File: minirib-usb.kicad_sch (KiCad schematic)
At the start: 59 parts, among them J1 USB_B_Micro, J2 Mini-DIN-6-Shielded, J3 RS232, Q1 MMBT3906, Q2 MMBT3904, Q3 MMBT3904, Q4 MMBT3904, Q5 MMBT3906, Q6 MMBT3904, Q7 MMBT3904, Q8 BSS138W, U1 FT231XS, U2 TL071, U3 MAX232

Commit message: initial revision D updates
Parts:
- removed C2, C6, C7, C8, C9: 1uF, Capacitor_SMD:C_0805_2012Metric_Pad1.18x1.45mm_HandSolder, symbol Device:C_Small
- removed C5: 0.1uF, Capacitor_SMD:C_0805_2012Metric_Pad1.18x1.45mm_HandSolder, symbol Device:C_Small
- removed D5, D6, D7: 1N4148, Diode_SMD:D_SOD-323_HandSoldering, symbol Device:D_Small
- removed Q1, Q5: MMBT3906, Package_TO_SOT_SMD:SOT-23, symbol Transistor_BJT:MMBT3906
- removed Q2, Q3, Q4, Q6, Q7: MMBT3904, Package_TO_SOT_SMD:SOT-23, symbol Transistor_BJT:MMBT3904
- removed R12, R14, R20: 10k, Resistor_SMD:R_0805_2012Metric_Pad1.20x1.40mm_HandSolder, symbol Device:R_Small
- removed R17: 4k7, Resistor_SMD:R_0805_2012Metric_Pad1.20x1.40mm_HandSolder, symbol Device:R_Small
- removed R18: 20k, Resistor_SMD:R_0805_2012Metric_Pad1.20x1.40mm_HandSolder, symbol Device:R_Small
- removed R21: 1k5, Resistor_SMD:R_0805_2012Metric_Pad1.20x1.40mm_HandSolder, symbol Device:R_Small
- removed U3: MAX232, Package_SO:SOIC-16W_7.5x10.3mm_P1.27mm, symbol max232:MAX232
- added H1, H2, H3, H4: MountingHole_Pad, MountingHole:MountingHole_2.7mm_M2.5_Pad_TopBottom, symbol Mechanical:MountingHole_Pad
- added J4: UART, Connector_PinHeader_2.54mm:PinHeader_1x05_P2.54mm_Vertical, symbol Connector:Conn_01x05_Female
- added Q1, Q2, Q4: BS84W, Package_TO_SOT_SMD:SOT-323_SC-70_Handsoldering, symbol Device:Q_PMOS_GSD
- added Q3, Q5, Q7: BSS138W, Package_TO_SOT_SMD:SOT-323_SC-70_Handsoldering, symbol Device:Q_NMOS_GSD
- J3: value RS232 -> UART
- R10, R9: value 9k1 -> 10k
- R11: value 47k -> 10k
- R13, R3: value 1k5 -> 10k
- R16: value 4k7 -> 10k
- R8: value 20k -> 10k
- renumbered C10 to C2, D8 to D5, D9 to D6, D10 to D7, D11 to D8, Q8 to Q6, R19 to R12, R22 to R14, R23 to R17, R24 to R18
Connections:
- net RXD_TTL is gone; now on net RXD: U1.4 (RXD)
- net TXD_TTL is gone; now on net TXD: U1.20 (TXD)
- net ~{CTS_TTL} is gone; now on net BUSY: U1.5 (~{RI}), U1.9 (~{CTS})
- net ~{DTR_TTL} is gone; now on net ~{DTR}: U1.1 (~{DTR})
- net +5V: now also R11.1, R16.2, R3.2, R9.2, Q1.2 (S), Q2.2 (S), Q4.2 (S); no longer R15.2
- net BUS+: now also R5.2, J4.2 (Pin_2), Q3.3 (D)
- net BUS-: now also R8.2, J4.1 (Pin_1), Q1.3 (D)
- net BUSY: now also J3.3 (Pin_3), R11.2, J4.4 (Pin_4), Q5.3 (D); no longer R15.1
- net GND: now also R10.1, R15.2, R4.1, R8.1, H1.1, H2.1, H3.1, H4.1, J4.5 (Pin_5), Q3.2 (S), Q5.2 (S), Q7.2 (S); no longer R11.2
- net RXD: now also R16.1, Q7.3 (D); no longer R3.1
- net TXD: now also R3.1, Q1.1 (G), Q2.1 (G); no longer R10.2, R9.2
- net ~{BUSY}: now also R10.2, R13.1, J4.3 (Pin_3), Q4.3 (D), Q5.1 (G)
- net at Q6.1 (G): now also R13.2
- net ~{DTR}: now reaches R9.1
- net ~{DTR}: now also J3.4 (Pin_4), Q4.1 (G); no longer R11.1
- net at R4.2: now also Q2.3 (D), Q3.1 (G); no longer R5.2
- net at U2.1: now also R15.1, Q7.1 (G); no longer R8.1
- removed net -8V: R13.2, R3.2
- removed net CTS: J3.4 (Pin_4), R13.1
- removed net DTR: J3.3 (Pin_3), R16.2
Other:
- note added: "BUS+ and BUS- are kept separate so they can be driven externally"
- note added: "BUS+ is idle high"
- note added: "BUS- is idle low"
- note added: "BUSY & CTS are idle high"
- note added: "RXD is idle high"
- note added: "TXD is idle high"
- note added: "~{BUSY} is idle low"
- note added: "~{DTR} is idle high"
- note removed: "UART to RS232 and +/- Regulators"
- moved on the sheet: D5, D6, D7, D8, J3, Q6, R12, R14, R17, R18, U2

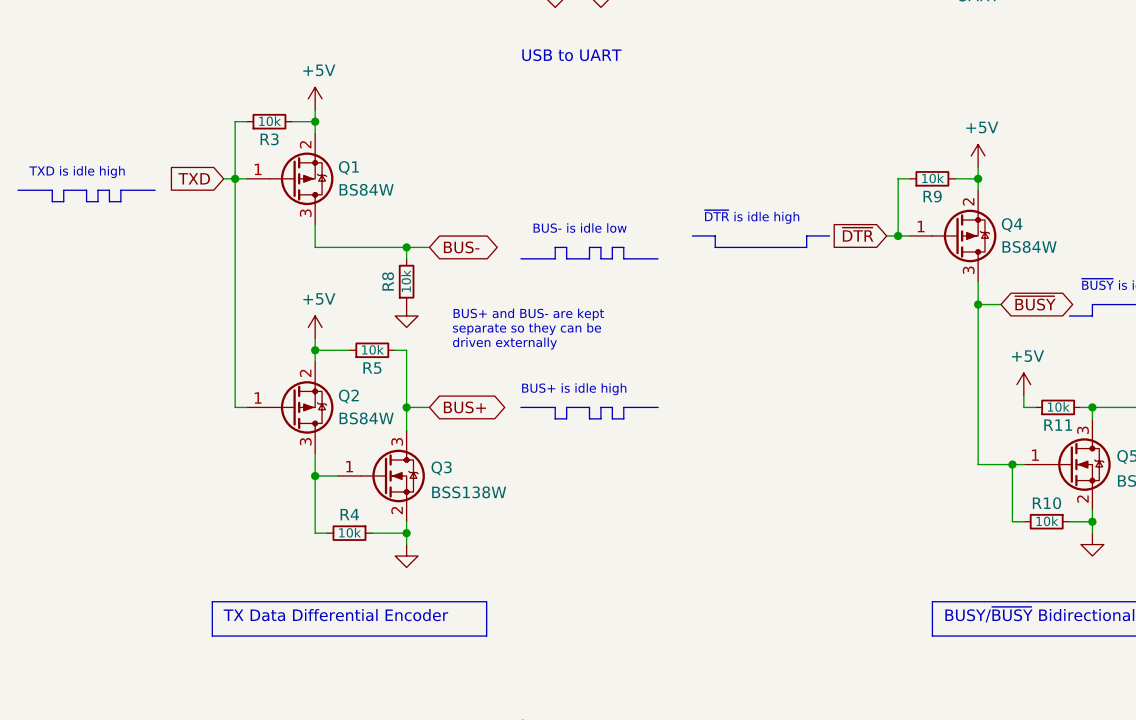
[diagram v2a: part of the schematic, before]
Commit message: revision E updates
added 10k resistors to TX & DTR lines from FT231XS to allow PFETs to turn off properly when TX/DTR at 3V3. Currently they're always on (oops)
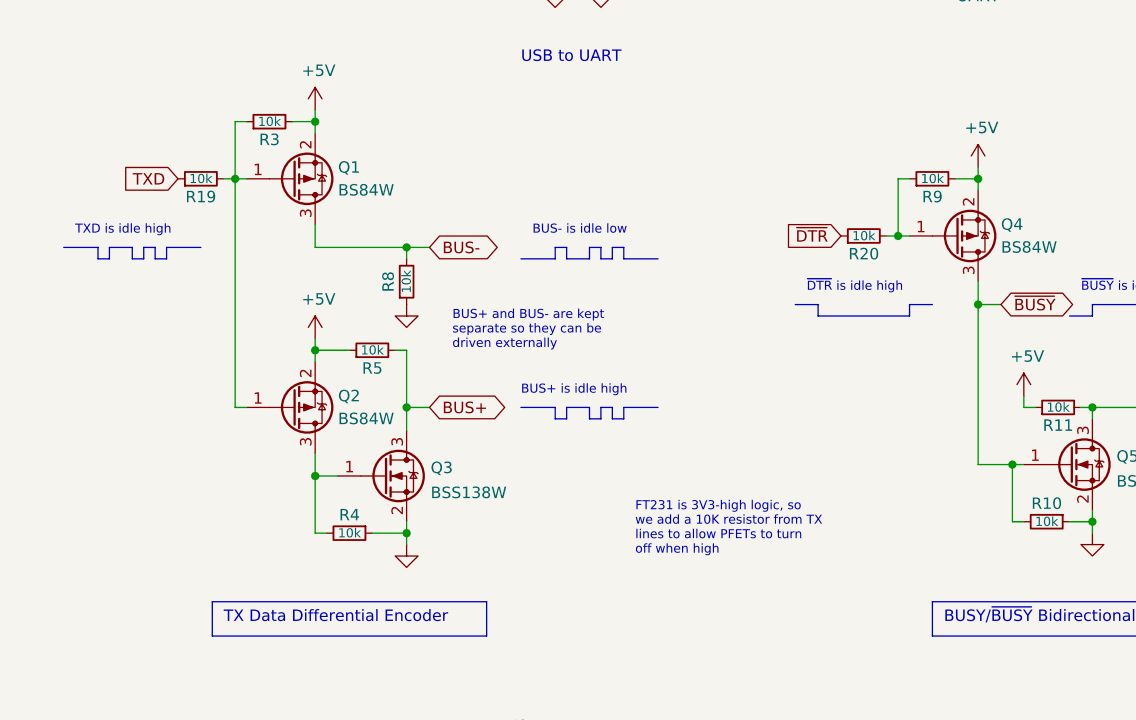
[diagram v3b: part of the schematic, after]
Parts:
- added R19, R20: 10k, Resistor_SMD:R_0805_2012Metric_Pad1.20x1.40mm_HandSolder, symbol Device:R_Small
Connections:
- net TXD: now also R19.1; no longer Q1.1 (G), Q2.1 (G), R3.1
- net ~{DTR}: now also R20.1; no longer Q4.1 (G), R9.1
- new net: Q1.1 (G), Q2.1 (G), R19.2, R3.1
- new net: Q4.1 (G), R20.2, R9.1
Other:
- note added: "FT231 is 3V3-high logic, so we add a 10K resistor from TX lines to allow PFETs to turn off when high"
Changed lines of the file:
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@@
   (title_block
     (title "MiniRIB-USB")
-    (date "2023-03-28")
-    (rev "D")
+    (date "2023-04-12")
+    (rev "E")
     (company "W3AXL")
     (comment 1 "USB based adaption of the RLN4008B schematic")
@@
     (stroke (width 0) (type solid) (color 0 0 0 0))
   )
-  (polyline (pts (xy 26.67 102.87) (xy 30.48 102.87))
+  (polyline (pts (xy 31.75 109.22) (xy 35.56 109.22))
     (stroke (width 0) (type solid) (color 0 0 0 0))
   )
@@
     (stroke (width 0) (type solid) (color 0 0 0 0))
   )
-  (polyline (pts (xy 30.48 102.87) (xy 30.48 104.14))
+  (polyline (pts (xy 35.56 109.22) (xy 35.56 110.49))
     (stroke (width 0) (type solid) (color 0 0 0 0))
   )
@@
     (stroke (width 0) (type default) (color 0 0 0 0))
   )
-  (polyline (pts (xy 38.1 104.14) (xy 38.1 102.87))
+  (polyline (pts (xy 43.18 110.49) (xy 43.18 109.22))
     (stroke (width 0) (type solid) (color 0 0 0 0))
   )
@@
     (stroke (width 0) (type default) (color 0 0 0 0))
   )
-  (polyline (pts (xy 104.14 109.22) (xy 114.3 109.22))
+  (polyline (pts (xy 115.57 116.84) (xy 125.73 116.84))
     (stroke (width 0) (type solid) (color 0 0 0 0))
   )
@@
     (stroke (width 0) (type default) (color 0 0 0 0))
   )
-  (polyline (pts (xy 34.29 104.14) (xy 35.56 104.14))
+  (polyline (pts (xy 39.37 110.49) (xy 40.64 110.49))
     (stroke (width 0) (type solid) (color 0 0 0 0))
   )
@@
     (stroke (width 0) (type default) (color 0 0 0 0))
   )
-  (polyline (pts (xy 36.83 104.14) (xy 38.1 104.14))
+  (polyline (pts (xy 41.91 110.49) (xy 43.18 110.49))
     (stroke (width 0) (type solid) (color 0 0 0 0))
   )
@@
     (stroke (width 0) (type default) (color 0 0 0 0))
   )
-  (polyline (pts (xy 30.48 104.14) (xy 31.75 104.14))
+  (polyline (pts (xy 35.56 110.49) (xy 36.83 110.49))
     (stroke (width 0) (type solid) (color 0 0 0 0))
   )
@@
     (stroke (width 0) (type default) (color 0 0 0 0))
   )
-  (polyline (pts (xy 104.14 107.95) (xy 104.14 109.22))
+  (polyline (pts (xy 115.57 115.57) (xy 115.57 116.84))
     (stroke (width 0) (type solid) (color 0 0 0 0))
   )
@@
     (stroke (width 0) (type default) (color 0 0 0 0))
   )
-  (polyline (pts (xy 114.3 107.95) (xy 116.84 107.95))
+  (polyline (pts (xy 125.73 115.57) (xy 128.27 115.57))
     (stroke (width 0) (type solid) (color 0 0 0 0))
   )
@@
     (stroke (width 0) (type default) (color 0 0 0 0))
   )
-  (polyline (pts (xy 114.3 109.22) (xy 114.3 107.95))
+  (polyline (pts (xy 125.73 116.84) (xy 125.73 115.57))
     (stroke (width 0) (type solid) (color 0 0 0 0))
   )
@@
     (stroke (width 0) (type default) (color 0 0 0 0))
   )
-  (polyline (pts (xy 36.83 102.87) (xy 36.83 104.14))
-    (stroke (width 0) (type solid) (color 0 0 0 0))
-  )
-  (polyline (pts (xy 101.6 107.95) (xy 104.14 107.95))
+  (polyline (pts (xy 41.91 109.22) (xy 41.91 110.49))
+    (stroke (width 0) (type solid) (color 0 0 0 0))
+  )
+  (polyline (pts (xy 113.03 115.57) (xy 115.57 115.57))
     (stroke (width 0) (type solid) (color 0 0 0 0))
   )
@@
     (stroke (width 0) (type solid) (color 0 0 0 0))
   )
-  (polyline (pts (xy 38.1 102.87) (xy 41.91 102.87))
+  (polyline (pts (xy 43.18 109.22) (xy 46.99 109.22))
     (stroke (width 0) (type solid) (color 0 0 0 0))
   )
@@
     (stroke (width 0) (type solid) (color 0 0 0 0))
   )
-  (polyline (pts (xy 34.29 102.87) (xy 34.29 104.14))
+  (polyline (pts (xy 39.37 109.22) (xy 39.37 110.49))
     (stroke (width 0) (type solid) (color 0 0 0 0))
   )
@@
     (stroke (width 0) (type default) (color 0 0 0 0))
   )
-  (polyline (pts (xy 31.75 104.14) (xy 31.75 102.87))
-    (stroke (width 0) (type solid) (color 0 0 0 0))
-  )
-  (polyline (pts (xy 31.75 102.87) (xy 34.29 102.87))
+  (polyline (pts (xy 36.83 110.49) (xy 36.83 109.22))
+    (stroke (width 0) (type solid) (color 0 0 0 0))
+  )
+  (polyline (pts (xy 36.83 109.22) (xy 39.37 109.22))
     (stroke (width 0) (type solid) (color 0 0 0 0))
   )
@@
     (stroke (width 0) (type solid) (color 0 0 0 0))
   )
-  (polyline (pts (xy 35.56 104.14) (xy 35.56 102.87))
+  (polyline (pts (xy 40.64 110.49) (xy 40.64 109.22))
     (stroke (width 0) (type solid) (color 0 0 0 0))
   )
@@
     (stroke (width 0) (type solid) (color 0 0 0 0))
   )
-  (polyline (pts (xy 35.56 102.87) (xy 36.83 102.87))
+  (polyline (pts (xy 40.64 109.22) (xy 41.91 109.22))
     (stroke (width 0) (type solid) (color 0 0 0 0))
   )
@@
     (effects (font (size 1.27 1.27)) (justify left bottom))
   )
+  (text "FT231 is 3V3-high logic, so \nwe add a 10K resistor from TX \nlines to allow PFETs to turn \noff when high"
+    (at 95.25 143.51 0)
+    (effects (font (size 1 1)) (justify left bottom))
+  )
   (text "BUS- is idle low" (at 83.82 107.95 0)
     (effects (font (size 1 1)) (justify left bottom))
@@
     (effects (font (size 1.27 1.27)) (justify left bottom))
   )
-  (text "~{DTR} is idle high" (at 102.87 106.68 0)
+  (text "~{DTR} is idle high" (at 114.3 114.3 0)
     (effects (font (size 1 1)) (justify left bottom))
   )
@@
     (effects (font (size 1 1)) (justify left bottom))
   )
-  (text "TXD is idle high" (at 27.94 101.6 0)
+  (text "TXD is idle high" (at 33.02 107.95 0)
     (effects (font (size 1 1)) (justify left bottom))
   )
@@
     )
   )
-  (global_label "~{DTR}" (shape input) (at 123.19 107.95 180) (fields_autoplaced)
+  (global_label "~{DTR}" (shape input) (at 118.11 107.95 180) (fields_autoplaced)
     (effects (font (size 1.27 1.27)) (justify right))
-    (property "Intersheet References" "${INTERSHEET_REFS}" (id 0) (at 117.3582 107.8706 0)
+    (property "Intersheet References" "${INTERSHEET_REFS}" (id 0) (at 112.2782 107.8706 0)
       (effects (font (size 1.27 1.27)) (justify right) hide)
     )
@@
     )
   )
-  (global_label "TXD" (shape input) (at 49.53 101.6 180) (fields_autoplaced)
+  (global_label "TXD" (shape input) (at 44.45 101.6 180) (fields_autoplaced)
     (effects (font (size 1.27 1.27)) (justify right))
-    (property "Intersheet References" "${INTERSHEET_REFS}" (id 0) (at 43.7587 101.6794 0)
+    (property "Intersheet References" "${INTERSHEET_REFS}" (id 0) (at 38.6787 101.6794 0)
       (effects (font (size 1.27 1.27)) (justify right) hide)
     )
@@
     (pin "1")
   )
+  (symbol (lib_id "Device:R_Small") (at 46.99 101.6 90) (unit 1)
+    (in_bom yes) (on_board yes)
+    (property "Reference" "R19" (id 0) (at 46.99 102.87 90)
+      (effects (font (size 1.27 1.27)) (justify bottom))
+    )
+    (property "Value" "10k" (id 1) (at 46.99 101.6 90)
+      (effects (font (size 1.016 1.016)))
+    )
+    (property "Footprint" "Resistor_SMD:R_0805_2012Metric_Pad1.20x1.40mm_HandSolder" (id 2) (at 46.99 101.6 0)
+      (effects (font (size 1.27 1.27)) hide)
+    )
+    (property "Datasheet" "~" (id 3) (at 46.99 101.6 0)
+      (effects (font (size 1.27 1.27)) hide)
+    )
+    (pin "1")
+    (pin "2")
+  )
   (symbol (lib_id "Connector:Conn_01x05_Female") (at 158.75 76.2 270) (unit 1)
     (in_bom yes) (on_board yes) (fields_autoplaced)
@@
     (pin "1")
   )
+  (symbol (lib_id "Device:R_Small") (at 120.65 107.95 90) (unit 1)
+    (in_bom yes) (on_board yes)
+    (property "Reference" "R20" (id 0) (at 120.65 109.22 90)
+      (effects (font (size 1.27 1.27)) (justify bottom))
+    )
+    (property "Value" "10k" (id 1) (at 120.65 107.95 90)
+      (effects (font (size 1.016 1.016)))
+    )
+    (property "Footprint" "Resistor_SMD:R_0805_2012Metric_Pad1.20x1.40mm_HandSolder" (id 2) (at 120.65 107.95 0)
+      (effects (font (size 1.27 1.27)) hide)
+    )
+    (property "Datasheet" "~" (id 3) (at 120.65 107.95 0)
+      (effects (font (size 1.27 1.27)) hide)
+    )
+    (pin "1")
+    (pin "2")
+  )
   (symbol (lib_id "power:GND") (at 222.25 128.27 0) (mirror y) (unit 1)
     (in_bom yes) (on_board yes)
@@
       (reference "R18") (unit 1) (value "1k5") (footprint "Resistor_SMD:R_0805_2012Metric_Pad1.20x1.40mm_HandSolder")
     )
+    (path "/1567824b-7649-4190-a466-b40ced8cc3bb"
+      (reference "R19") (unit 1) (value "10k") (footprint "Resistor_SMD:R_0805_2012Metric_Pad1.20x1.40mm_HandSolder")
+    )
+    (path "/4e30c4e8-ba04-4278-b89b-73fa8d4eb10f"
+      (reference "R20") (unit 1) (value "10k") (footprint "Resistor_SMD:R_0805_2012Metric_Pad1.20x1.40mm_HandSolder")
+    )
     (path "/05e35eed-caa5-46eb-845c-7d9c2ab69c48"
